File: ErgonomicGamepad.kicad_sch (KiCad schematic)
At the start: 84 parts, among them J1 USB_C_Receptacle_USB2.0_16P, J2 Conn_01x08, J3 Conn_01x08, J4 Conn_01x08, J5 AVR-ISP-6, J6 Conn_01x08, J7 1824417, SW01 SW_DIP_x01, SW02 SW_DIP_x01, SW03 SW_DIP_x01, SW04 SW_DIP_x01, SW05 SW_DIP_x01, SW06 SW_DIP_x01, SW07 SW_DIP_x01, SW08 SW_DIP_x01, SW09 SW_DIP_x01, SW10 SW_DIP_x01, SW11 SW_DIP_x01, SW12 SW_DIP_x01, SW13 SW_DIP_x01, SW14 SW_DIP_x01, SW15 SW_DIP_x01, SW16 SW_DIP_x01, SW17 SW_DIP_x01, SW18 SW_DIP_x01, SW19 SW_DIP_x01, SW20 SW_DIP_x01, SW21 SW_DIP_x01, SW22 SW_DIP_x01, SW23 SW_DIP_x01, SW24 SW_DIP_x01, U1 ATmega32U4-A, U2 USBLC6-2SC6, Y1 Crystal

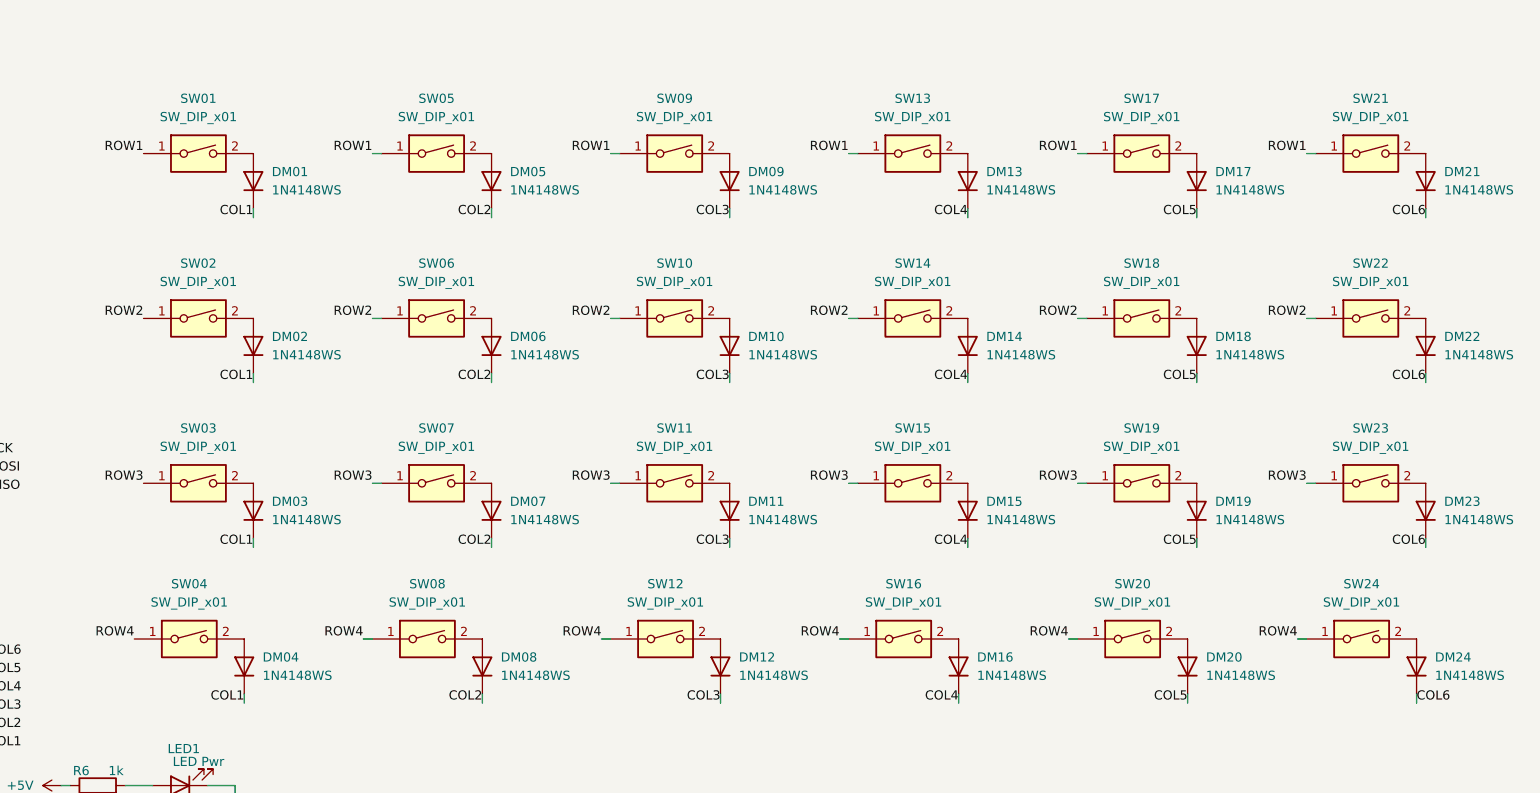
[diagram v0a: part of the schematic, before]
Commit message: schematic+docs: specify SW01-24 hotswap sockets, mark DNP, document hand-sourcing
SW01-24 backfilled with Kailh CPG151101S11-16 (LCSC C5156480), the
closed-ring hotswap socket variant. Set DNP=yes (in_bom stays yes) so
JLCPCB fabricates the correct pads/holes but skips auto-placement,
since this part shows near-zero LCSC stock.

README: documents hand-sourcing for the sockets, the Cherry MX Brown
switches that plug into them, and keycaps, plus where to actually buy
the sockets (AliExpress small-quantity listings or splitkb.com) since
LCSC/JLCPCB isn't a reliable channel for this part category. Also
fixed a stale footprint reference for SWR1.

Co-Authored-By: Claude Sonnet 5 <noreply@anthropic.com>
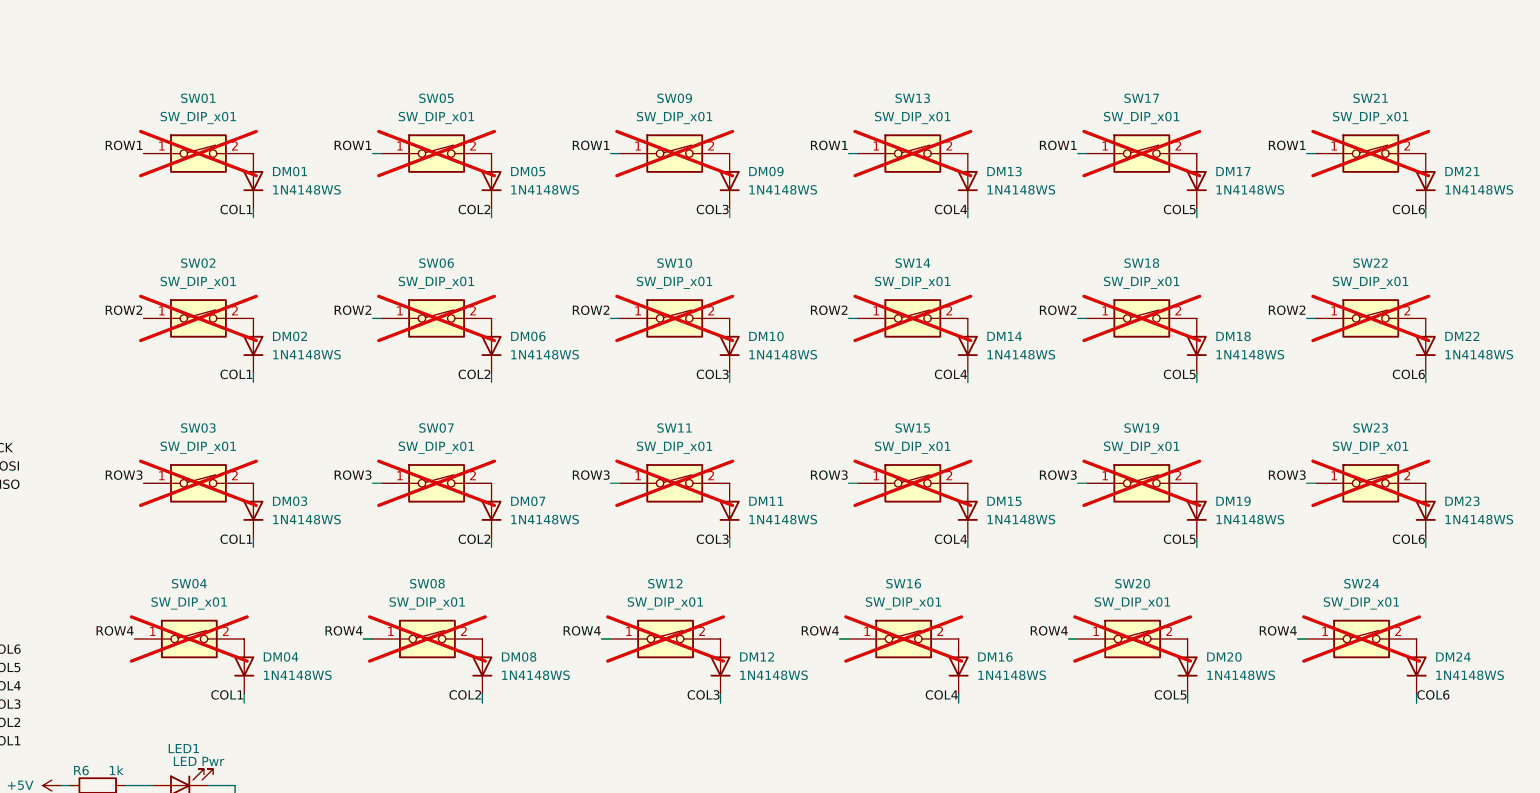
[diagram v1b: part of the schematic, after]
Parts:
- SW01, SW02, SW03, SW04, SW05, SW06, SW07, SW08, SW09, SW10, SW11, SW12, SW13, SW14, SW15, SW16, SW17, SW18, SW19, SW20, SW21, SW22, SW23, SW24: LCSC (none) -> C5156480; MPN (none) -> CPG151101S11-16; Manufacturer (none) -> Kailh; now not fitted
